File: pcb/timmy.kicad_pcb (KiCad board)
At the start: 4 copper layers, 66 x 86 mm, 38 parts, among them SW1 SW_Push, SW10 RotaryEncoder_Switch, SW11 RotaryEncoder_Switch, SW2 SW_Push, SW3 SW_Push, SW4 SW_Push, SW5 SW_Push, SW6 SW_Push, SW7 SW_Push, SW8 SW_Push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

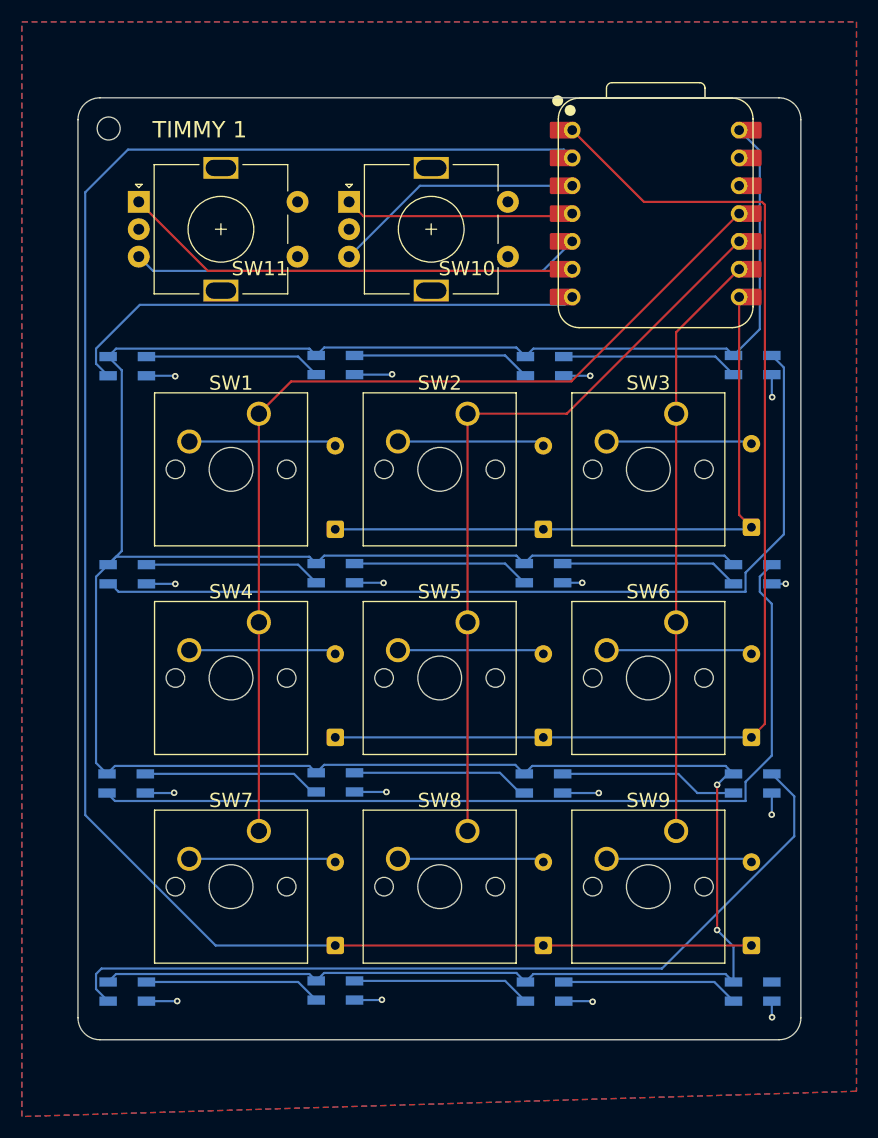
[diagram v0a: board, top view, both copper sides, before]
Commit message: update to accomodate back-mounted LEDs
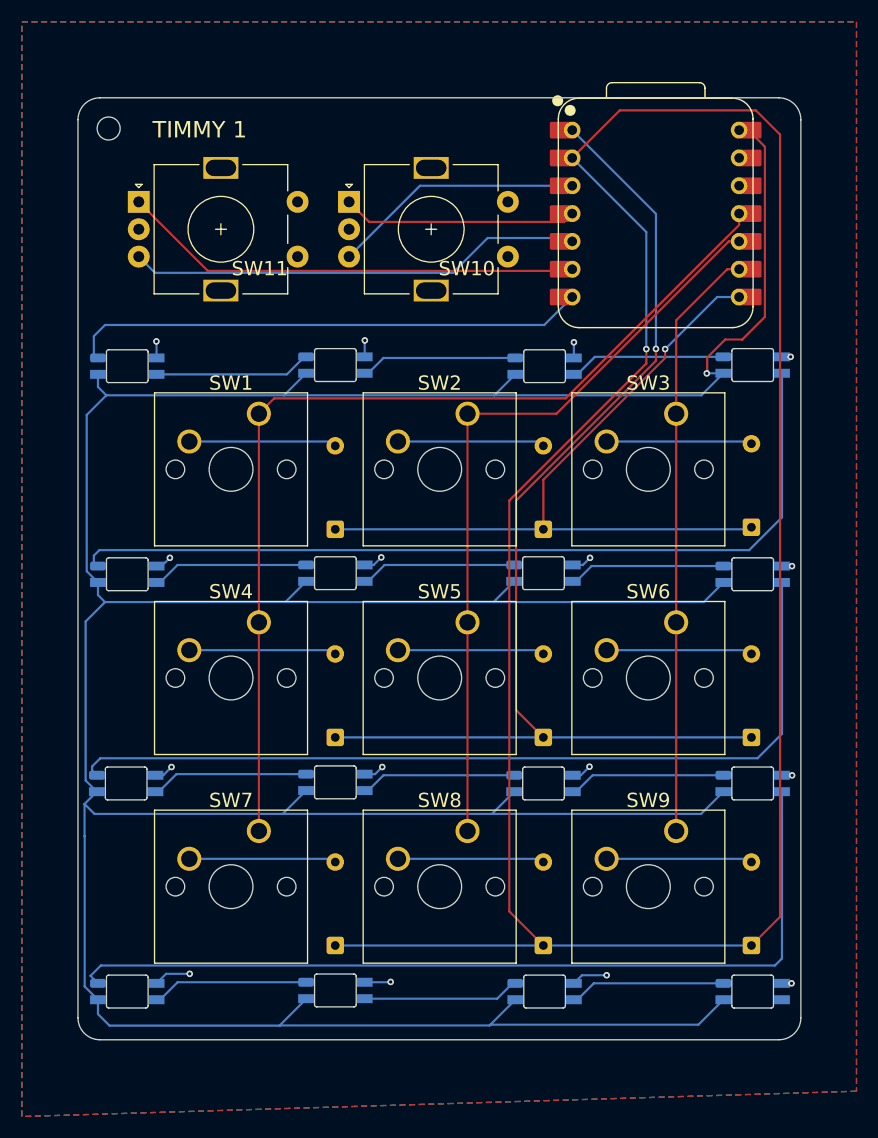
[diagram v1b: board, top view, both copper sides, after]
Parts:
- D1, D12, D13, D14, D15, D16, D17, D18, D19, D2, D20, D21, D22, D23, D24, D25: footprint LED_SMD:LED_SK6812MINI_PLCC4_3.5x3.5mm_P1.75mm -> libraries:sk6812-mini-e
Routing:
- net Row 2: track 169.0 -> 216.0 mm, vias 0 -> 1
- net +5V: track 318.6 -> 346.5 mm, vias 2 -> 1
- net GND: track 39.2 -> 27.7 mm
- net Row 0: track 59.6 -> 67.9 mm, vias 0 -> 1
- net Row 1: track 107.6 -> 102.9 mm, vias 0 -> 1
- net Net-(D17-DOUT): track 82.1 -> 79.0 mm
- net Net-(D13-DOUT): track 81.1 -> 78.5 mm
- net Net-(D23-DOUT): track 16.4 -> 14.3 mm
- net Net-(D19-DOUT): track 16.3 -> 14.2 mm
- net Net-(D16-DOUT): track 16.4 -> 14.3 mm
- net Net-(D12-DIN): track 16.4 -> 14.3 mm
- net Net-(D24-DOUT): track 16.2 -> 14.3 mm
- net Net-(D20-DOUT): track 16.3 -> 14.4 mm
- net Net-(D15-DOUT): track 16.2 -> 14.3 mm
- net Net-(D12-DOUT): track 16.2 -> 14.3 mm
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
